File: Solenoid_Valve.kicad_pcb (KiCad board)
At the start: 2 copper layers, 84.3 x 41.6 mm, 58 parts, among them IC1 Si8621AB-B-ISR, J1 Conn_01x02, J10 Conn_01x05, J11 Conn_01x02, J12 Conn_01x02, J13 Conn_01x02, J14 Conn_01x02, J15 Conn_01x02, J16 Conn_01x02, J17 Conn_01x02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

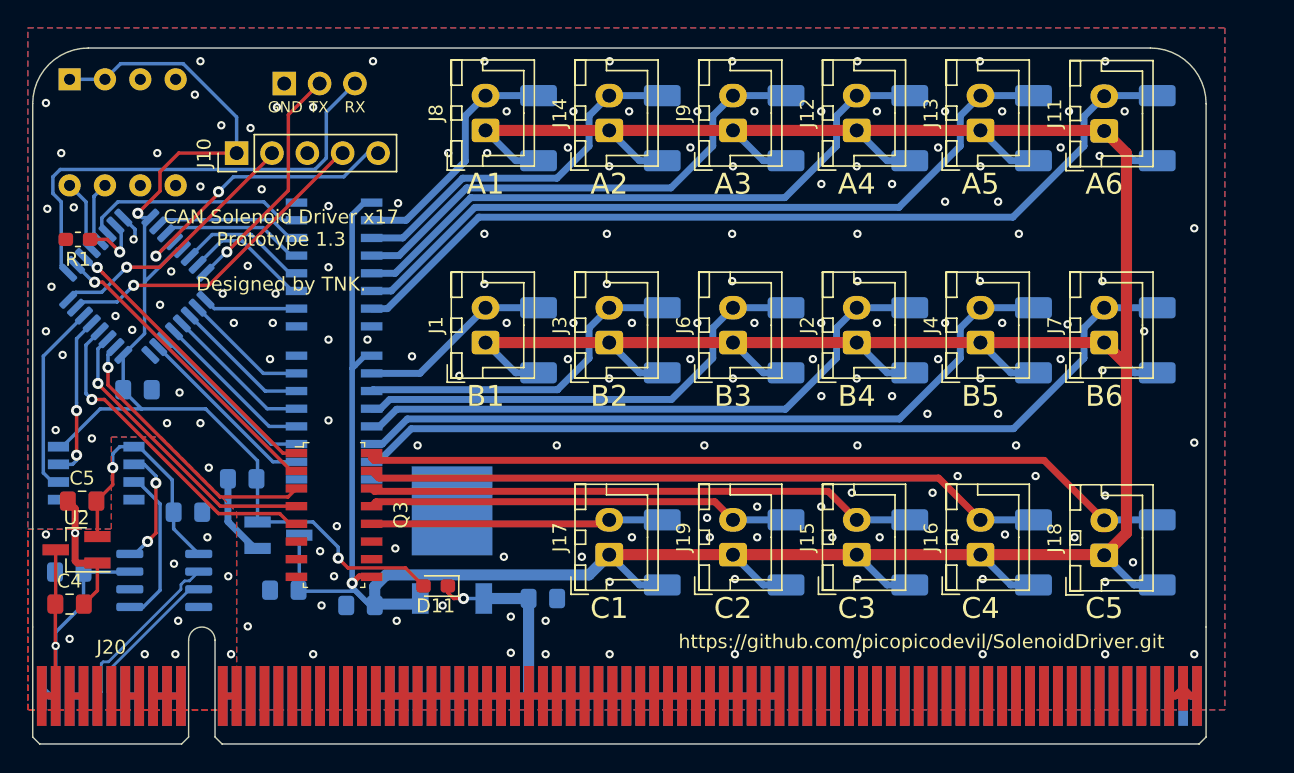
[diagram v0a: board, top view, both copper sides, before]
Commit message: Update: フットプリントライブラリの変更
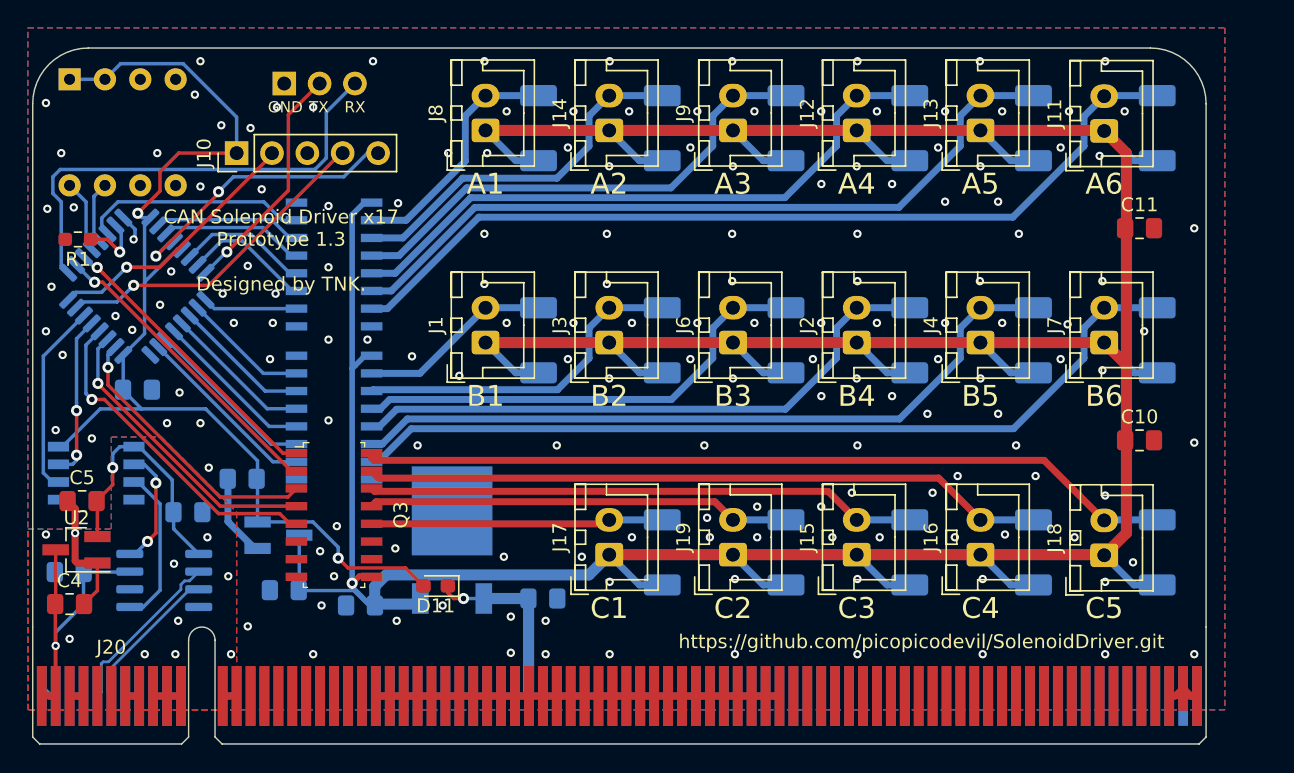
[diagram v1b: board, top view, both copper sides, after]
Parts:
- added C10: 10u, Capacitor_SMD:C_0805_2012Metric_Pad1.18x1.45mm_HandSolder, F.Cu at (229.9, 127.6)
- added C11: 10u, Capacitor_SMD:C_0805_2012Metric_Pad1.18x1.45mm_HandSolder, F.Cu at (229.9, 112.4)
- C1, C2, C3, C4, C5, C6, C7, C9: footprint Capacitor_SMD:C_0805_2012Metric_Pad1.15x1.40mm_HandSolder -> Capacitor_SMD:C_0805_2012Metric_Pad1.18x1.45mm_HandSolder
- C8: value 4.7u -> 2.2u; footprint Capacitor_SMD:C_0805_2012Metric_Pad1.15x1.40mm_HandSolder -> Capacitor_SMD:C_0805_2012Metric_Pad1.18x1.45mm_HandSolder
- R1: footprint Resistor_SMD:R_0603_1608Metric_Pad1.05x0.95mm_HandSolder -> Resistor_SMD:R_0603_1608Metric_Pad0.98x0.95mm_HandSolder
